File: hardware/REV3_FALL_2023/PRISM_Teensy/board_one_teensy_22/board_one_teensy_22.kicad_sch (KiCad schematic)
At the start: 19 parts, among them J1 DM3CS-SF, J2 PRISM_IO_INTERFACE, U1 Teensy4.0, U2 BNO055_Breakout, U3 3966

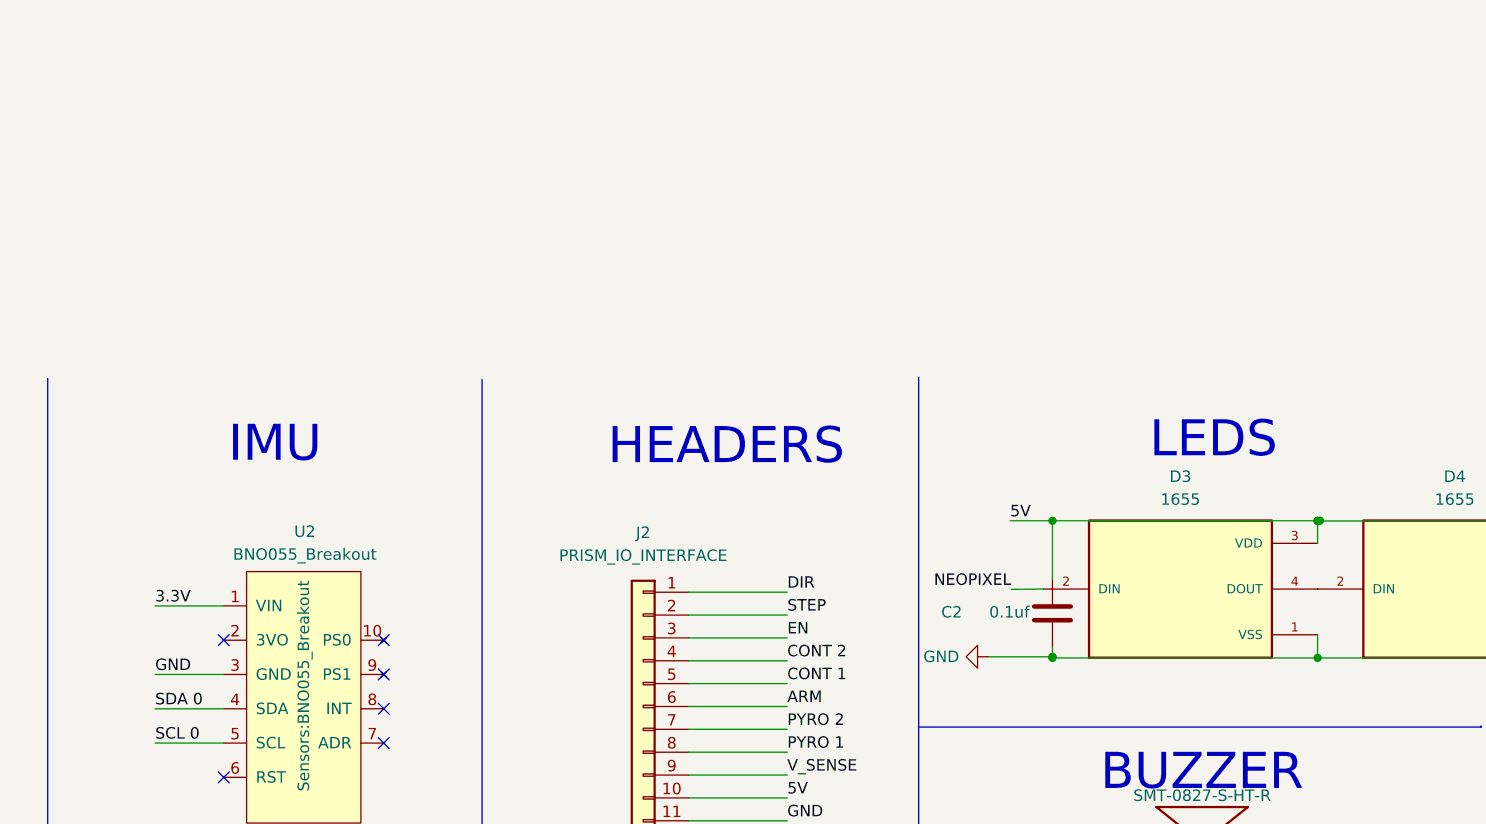
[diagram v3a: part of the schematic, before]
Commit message: added new IMU footprint + symbol
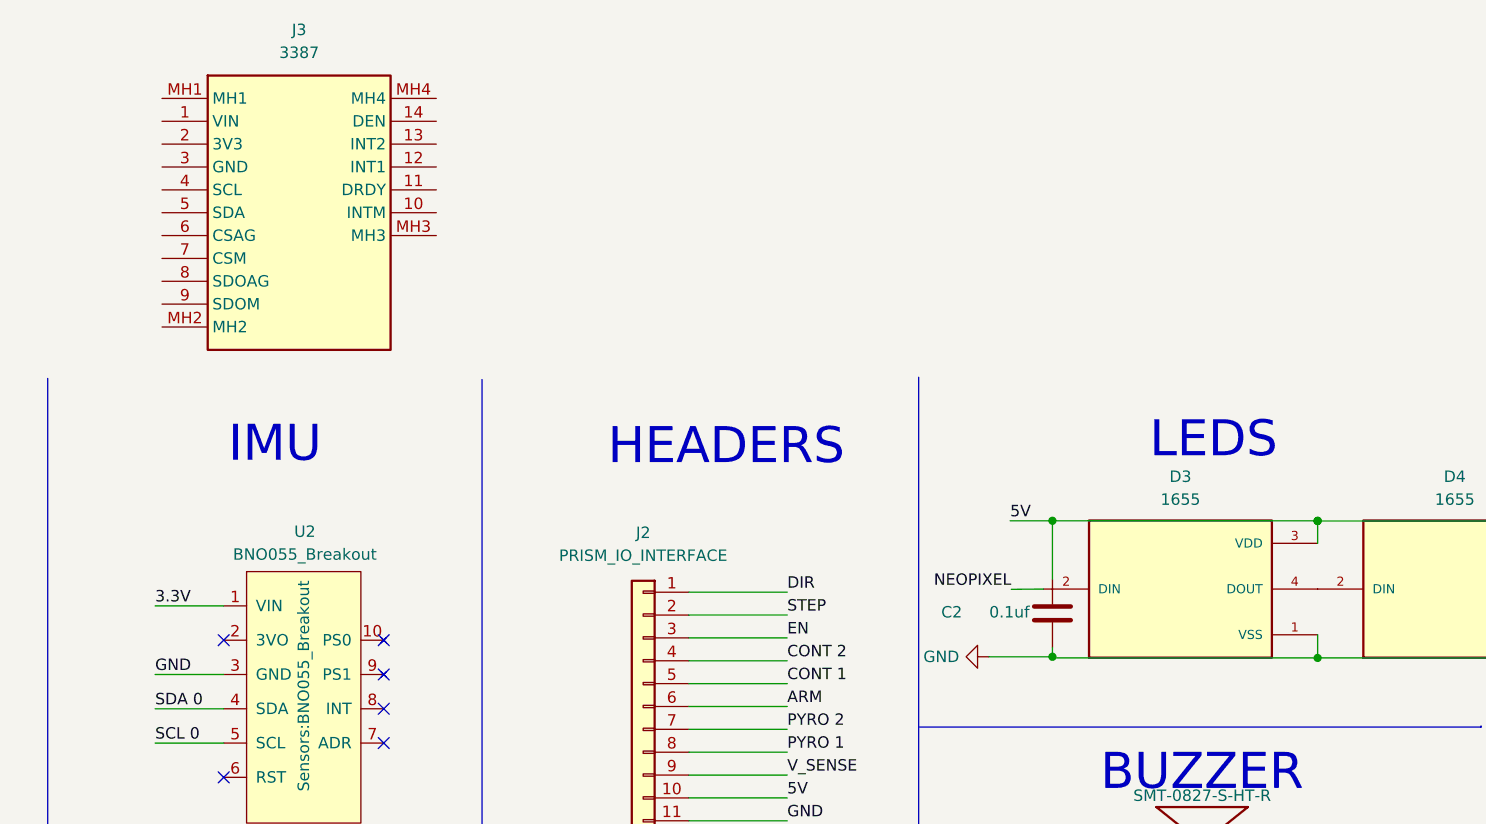
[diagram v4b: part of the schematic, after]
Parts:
- added J3: 3387, 3387, symbol LSM9DS1:3387

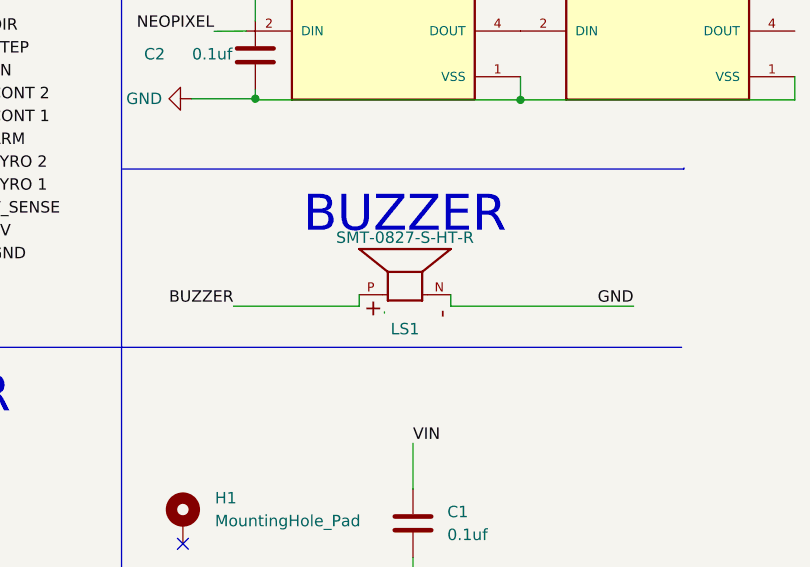
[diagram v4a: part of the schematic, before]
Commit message: new buzzer replaced
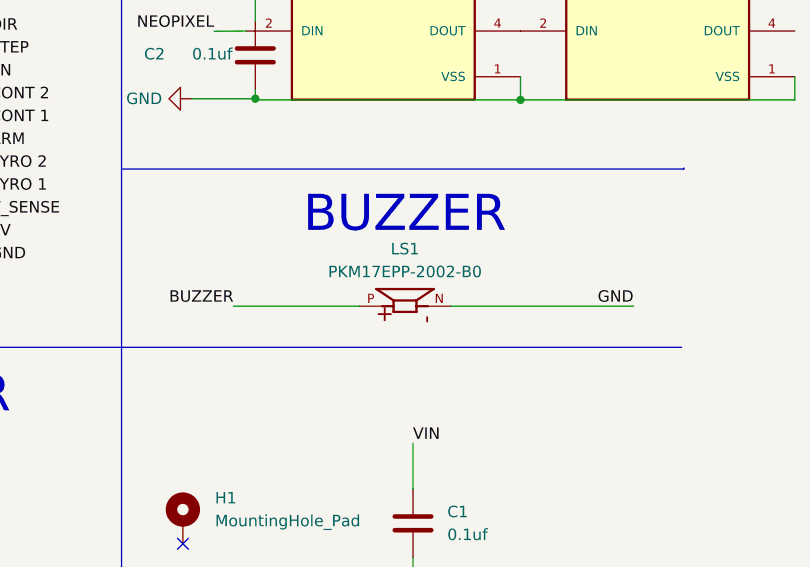
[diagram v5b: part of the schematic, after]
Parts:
- removed LS1: SMT-0827-S-HT-R, buzzer:XDCR_SMT-0827-S-HT-R, symbol Device:SMT-0827-S-HT-R
- added LS1: PKM17EPP-2002-B0, PKM17EPP-2002-B0:SPKR_PKM17EPP-2002-B0, symbol PKM:PKM17EPP-2002-B0
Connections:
- net BUZZER: now also LS1.P
- net GND: now also LS1.N
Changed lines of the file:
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@@
-    (stroke (width 0) (type default))
-  )
-  (wire (pts (xy 259.08 66.04) (xy 259.08 64.77))
-    (stroke (width 0) (type default))
-  )
-  (wire (pts (xy 251.714 66.675) (xy 251.714 66.802))
     (stroke (width 0) (type default))
   )
@@
   )
   (wire (pts (xy 196.977 35.814) (xy 207.899 35.814))
-    (stroke (width 0) (type default))
-  )
-  (wire (pts (xy 248.92 66.04) (xy 248.92 64.77))
     (stroke (width 0) (type default))
   )
@@
     )
   )
-  (symbol (lib_id "Device:SMT-0827-S-HT-R") (at 254 62.23 90) (unit 1)
-    (in_bom yes) (on_board yes) (dnp no)
-    (property "Reference" "LS1" (at 254 68.58 90)
-      (effects (font (size 1.27 1.27)))
-    )
-    (property "Value" "SMT-0827-S-HT-R" (at 254 58.42 90)
-      (effects (font (size 1.27 1.27)))
-    )
-    (property "Footprint" "buzzer:XDCR_SMT-0827-S-HT-R" (at 242.57 62.23 0)
-      (effects (font (size 1.27 1.27)) (justify bottom) hide)
-    )
-    (property "Datasheet" "" (at 254 62.23 0)
-      (effects (font (size 1.27 1.27)) hide)
-    )
-    (property "STANDARD" "Manufacturer Recommendations" (at 243.84 62.23 0)
-      (effects (font (size 1.27 1.27)) (justify bottom) hide)
-    )
-    (property "MAXIMUM_PACKAGE_HEIGHT" "3.3mm" (at 237.49 63.5 0)
-      (effects (font (size 1.27 1.27)) (justify bottom) hide)
-    )
-    (property "MANUFACTURER" "PUI Audio" (at 238.76 63.5 0)
-      (effects (font (size 1.27 1.27)) (justify bottom) hide)
-    )
-    (property "PARTREV" "31/03/20" (at 240.03 63.5 0)
+  (symbol (lib_id "Mechanical:MountingHole") (at 229.5755 103.3669 0) (unit 1)
+    (in_bom yes) (on_board yes) (dnp no) (fields_autoplaced)
+    (property "Reference" "H2" (at 232.8775 102.0968 0)
+      (effects (font (size 1.27 1.27)) (justify left))
+    )
+    (property "Value" "MountingHole" (at 232.8775 104.6368 0)
+      (effects (font (size 1.27 1.27)) (justify left))
+    )
+    (property "Footprint" "MountingHole:MountingHole_3.2mm_M3_DIN965_Pad_TopBottom" (at 229.5755 103.3669 0)
+      (effects (font (size 1.27 1.27)) hide)
+    )
+    (property "Datasheet" "~" (at 229.5755 103.3669 0)
+      (effects (font (size 1.27 1.27)))
+    )
+    (instances
+      (project "board_one_teensy_22"
+        (path "/7a48c3b0-2761-409e-ae2f-7ebae3820225"
+          (reference "H2") (unit 1)
+        )
+      )
+    )
+  )
+  (symbol (lib_id "PKM:PKM17EPP-2002-B0") (at 254 66.04 90) (unit 1)
+    (in_bom yes) (on_board yes) (dnp no) (fields_autoplaced)
+    (property "Reference" "LS1" (at 254 59.69 90)
+      (effects (font (size 1.27 1.27)))
+    )
+    (property "Value" "PKM17EPP-2002-B0" (at 254 62.23 90)
+      (effects (font (size 1.27 1.27)))
+    )
+    (property "Footprint" "PKM17EPP-2002-B0:SPKR_PKM17EPP-2002-B0" (at 254 66.04 0)
+      (effects (font (size 1.27 1.27)) (justify bottom) hide)
+    )
+    (property "Datasheet" "" (at 254 66.04 0)
+      (effects (font (size 1.27 1.27)) hide)
+    )
+    (property "MF" "Murata Electronics" (at 254 66.04 0)
+      (effects (font (size 1.27 1.27)) (justify bottom) hide)
+    )
+    (property "MAXIMUM_PACKAGE_HEIGHT" "9.8 mm" (at 254 66.04 0)
+      (effects (font (size 1.27 1.27)) (justify bottom) hide)
+    )
+    (property "Package" "Radial-2 Murata" (at 254 66.04 0)
+      (effects (font (size 1.27 1.27)) (justify bottom) hide)
+    )
+    (property "Price" "None" (at 254 66.04 0)
+      (effects (font (size 1.27 1.27)) (justify bottom) hide)
+    )
+    (property "Check_prices" "https://www.snapeda.com/parts/PKM17EPP-2002-B0/Murata+Electronics+North+America/view-part/?ref=eda" (at 254 66.04 0)
+      (effects (font (size 1.27 1.27)) (justify bottom) hide)
+    )
+    (property "STANDARD" "IPC-7351B" (at 254 66.04 0)
+      (effects (font (size 1.27 1.27)) (justify bottom) hide)
+    )
+    (property "PARTREV" "August 1, 2017" (at 254 66.04 0)
+      (effects (font (size 1.27 1.27)) (justify bottom) hide)
+    )
+    (property "SnapEDA_Link" "https://www.snapeda.com/parts/PKM17EPP-2002-B0/Murata+Electronics+North+America/view-part/?ref=snap" (at 254 66.04 0)
+      (effects (font (size 1.27 1.27)) (justify bottom) hide)
+    )
+    (property "MP" "PKM17EPP-2002-B0" (at 254 66.04 0)
+      (effects (font (size 1.27 1.27)) (justify bottom) hide)
+    )
+    (property "Purchase-URL" "https://www.snapeda.com/api/url_track_click_mouser/?unipart_id=293922&manufacturer=Murata Electronics&part_name=PKM17EPP-2002-B0&search_term=3v buzzer" (at 254 66.04 0)
+      (effects (font (size 1.27 1.27)) (justify bottom) hide)
+    )
+    (property "Description" "\nBuzzers Transducer, Externally Driven Piezo 3 V - 2kHz 70dB @ 3V, 10cm Through Hole PC Pins\n" (at 254 66.04 0)
+      (effects (font (size 1.27 1.27)) (justify bottom) hide)
+    )
+    (property "Availability" "In Stock" (at 254 66.04 0)
+      (effects (font (size 1.27 1.27)) (justify bottom) hide)
+    )
+    (property "MANUFACTURER" "Murata Electronics" (at 254 66.04 0)
       (effects (font (size 1.27 1.27)) (justify bottom) hide)
     )
@@
         )
       )
-    )
-  )
-  (symbol (lib_id "Mechanical:MountingHole") (at 229.5755 103.3669 0) (unit 1)
-    (in_bom yes) (on_board yes) (dnp no) (fields_autoplaced)
-    (property "Reference" "H2" (at 232.8775 102.0968 0)
-      (effects (font (size 1.27 1.27)) (justify left))
-    )
-    (property "Value" "MountingHole" (at 232.8775 104.6368 0)
-      (effects (font (size 1.27 1.27)) (justify left))
-    )
-    (property "Footprint" "MountingHole:MountingHole_3.2mm_M3_DIN965_Pad_TopBottom" (at 229.5755 103.3669 0)
-      (effects (font (size 1.27 1.27)) hide)
-    )
-    (property "Datasheet" "~" (at 229.5755 103.3669 0)
-      (effects (font (size 1.27 1.27)))
-    )
-    (instances
-      (project "board_one_teensy_22"
-        (path "/7a48c3b0-2761-409e-ae2f-7ebae3820225"
-          (reference "H2") (unit 1)
-        )
-      )

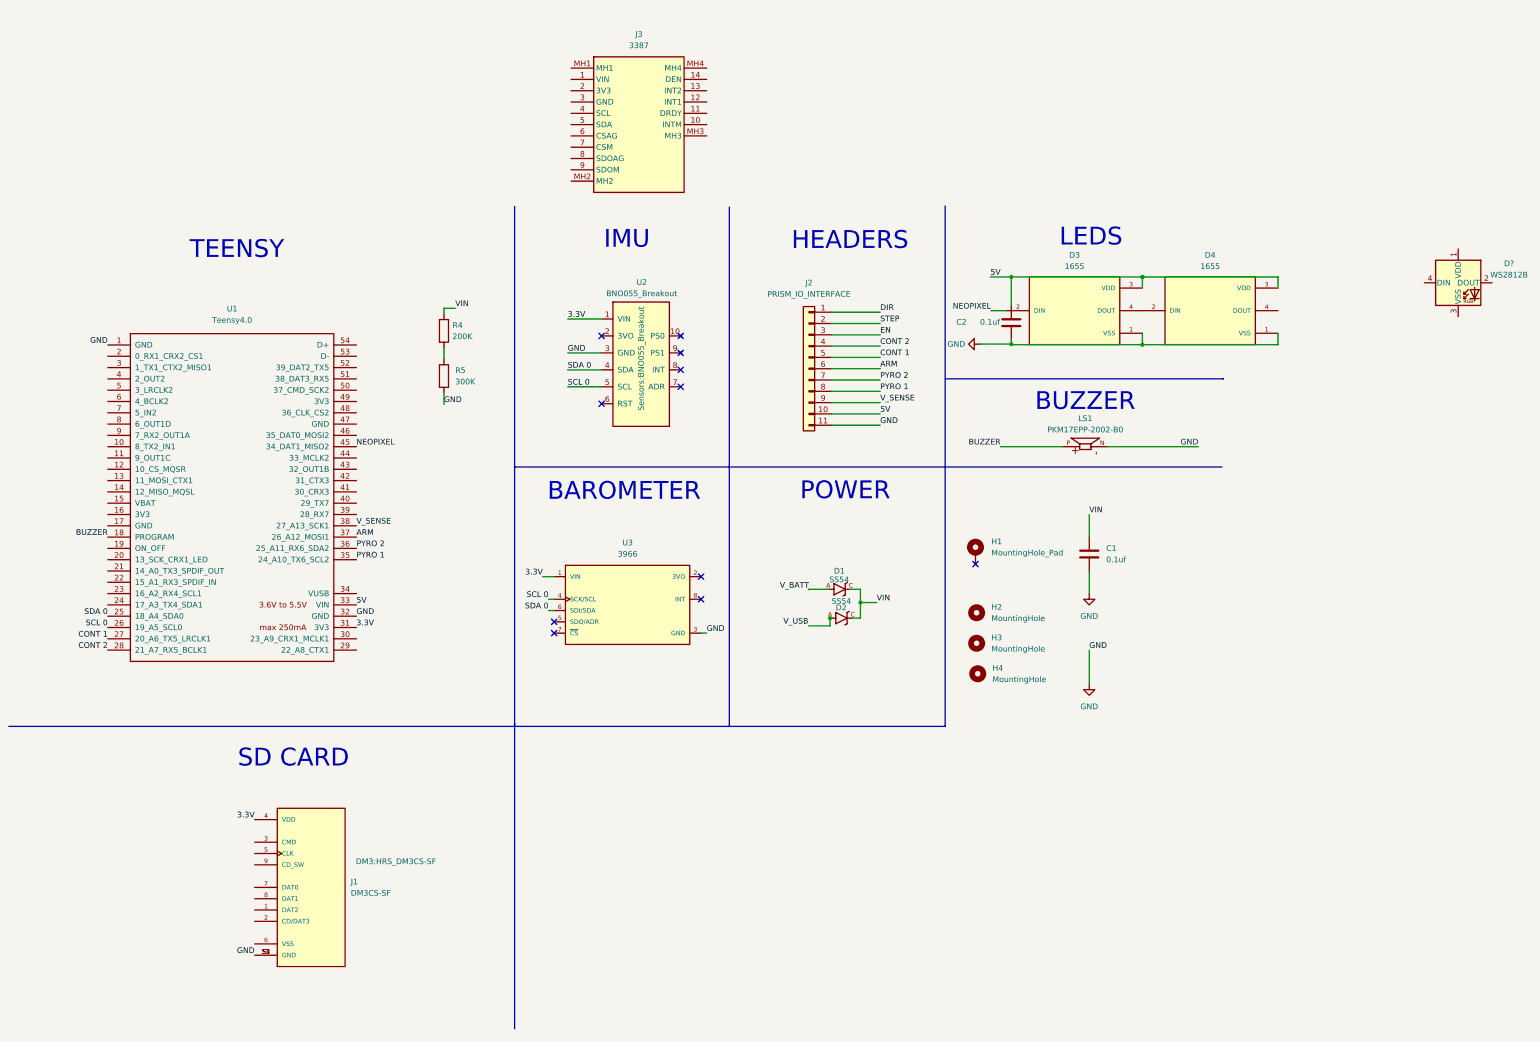
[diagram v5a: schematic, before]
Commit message: new IMU wired
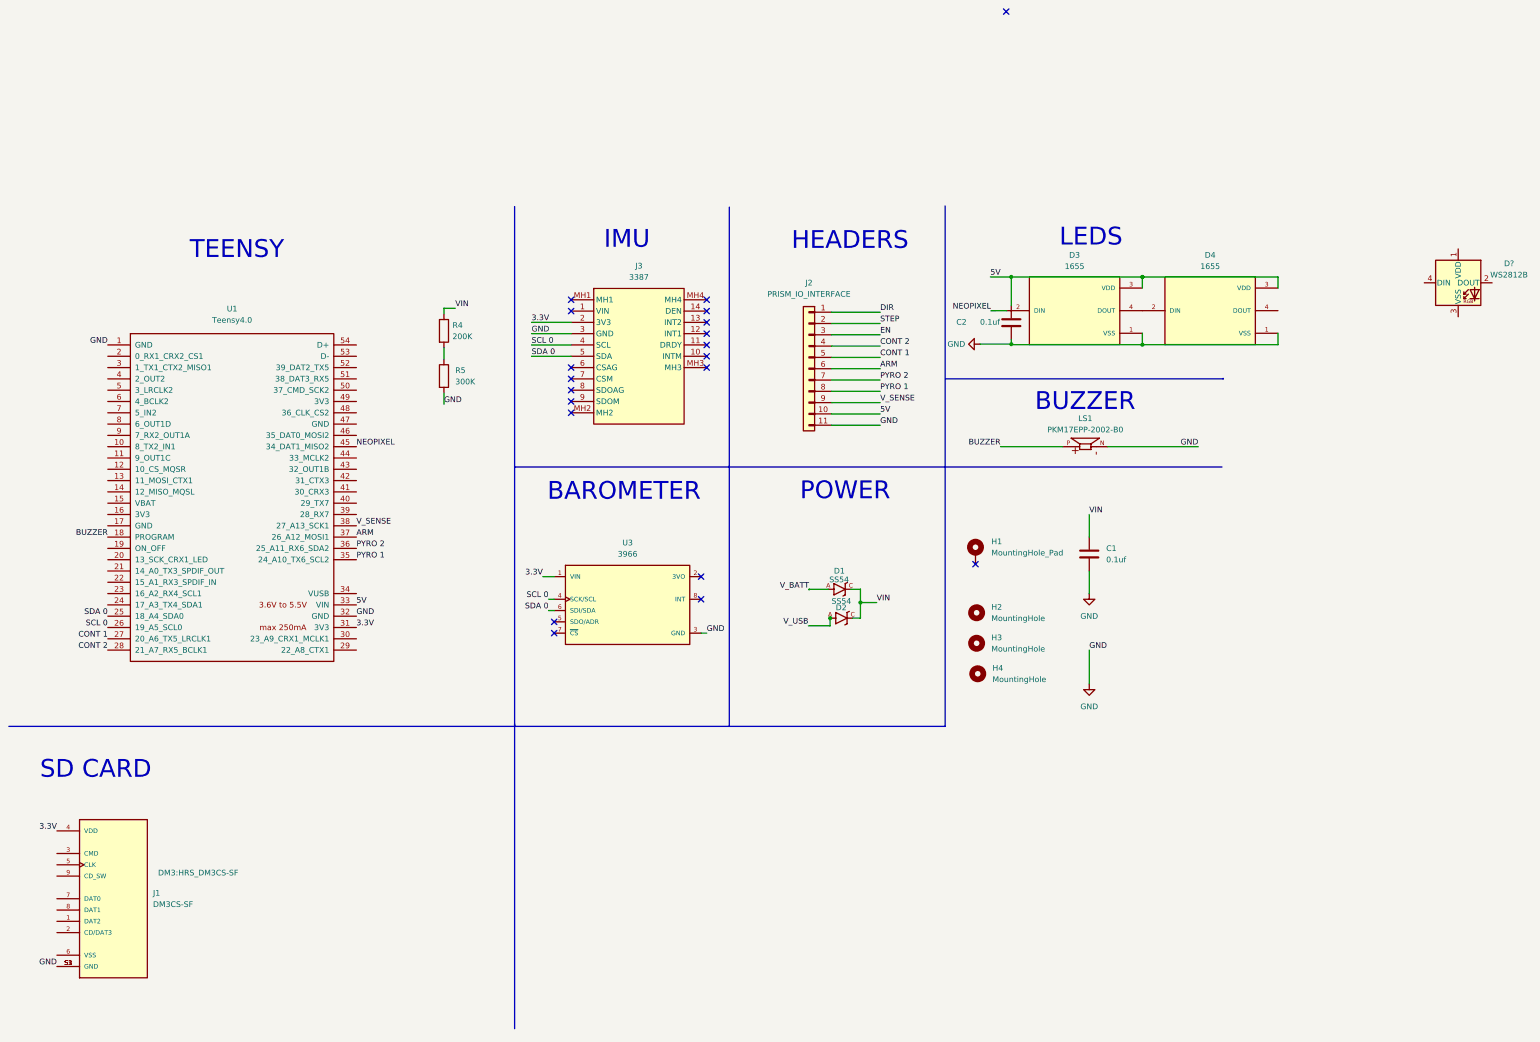
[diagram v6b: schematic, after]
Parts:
- removed U2: BNO055_Breakout, Sensors:BNO055_Breakout, symbol REV2_SPRING_2022-rescue:BNO055_Breakout-Sensors_2021_2022
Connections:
- net 3.3V: now also J3.2 (3V3)
- net GND: now also J3.3 (GND)
- net SCL 0: now also J3.4 (SCL)
- net SDA 0: now also J3.5 (SDA)
- no-connect marks 11 -> 20
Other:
- moved on the sheet: J1, J3

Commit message: moving GPS and Radio to main
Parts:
- added U2: GPS-14414, GPS_layout:GPS-14414, symbol GPS:GPS-14414
- added U4: RFM69HCW_Breakout, Sensors:RFM69HCW_Breakout, symbol sensors:RFM69HCW_Breakout
- gave numbers to parts that had none: 1
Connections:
- net 3.3V: now also U2.3 (3.3V), U4.1 (VIN)
- net GND: now also U2.2 (GND), U4.2 (GND)
- new net CS 1: U4.8 (CS)
- new net MISO: U4.6 (MISO)
- new net MOSI: U4.7 (MOSI)
- new net RX 5: U4.4 (G0)
- new net SCK: U4.5 (SCK)
- new net SCL 1: U2.5 (SCL)
- new net SDA 1: U2.4 (SDA)
- new net TX 5: U4.9 (RST)
- no-connect marks 20 -> 32
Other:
- note added: "GPS"
- note added: "Radio"
